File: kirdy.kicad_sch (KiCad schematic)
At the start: 0 parts

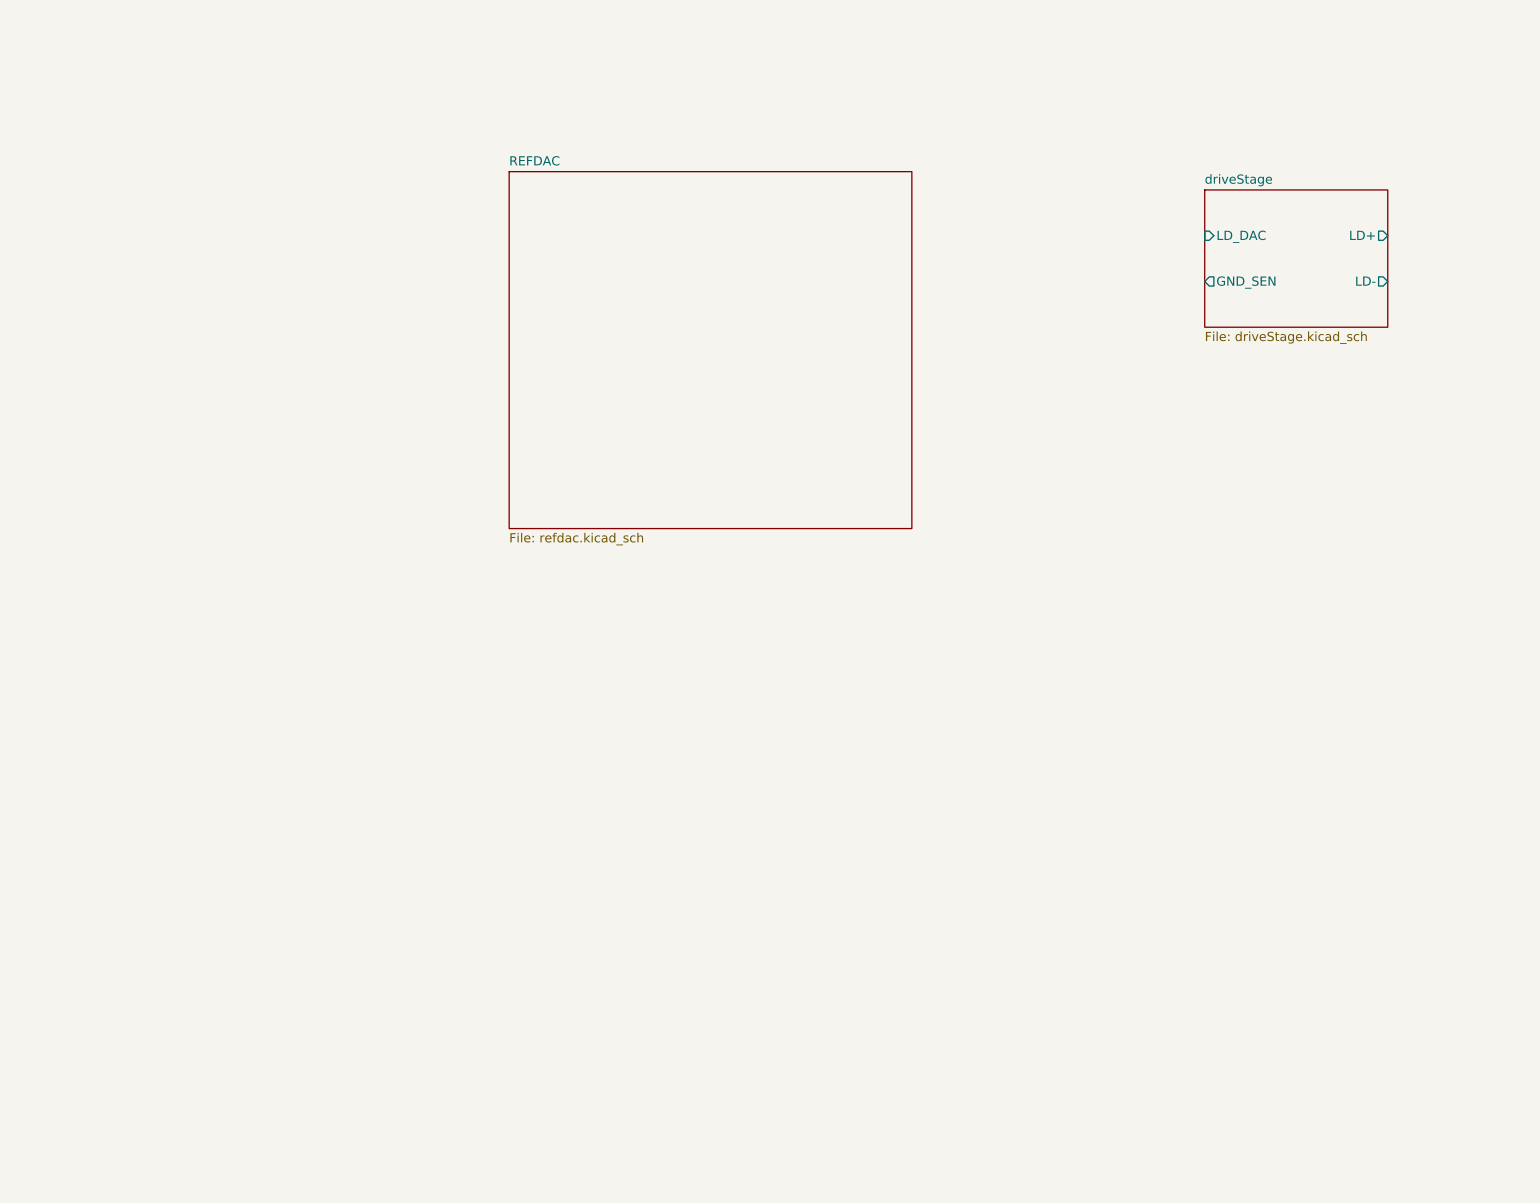
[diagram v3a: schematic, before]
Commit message: finish drive stage, add sheets
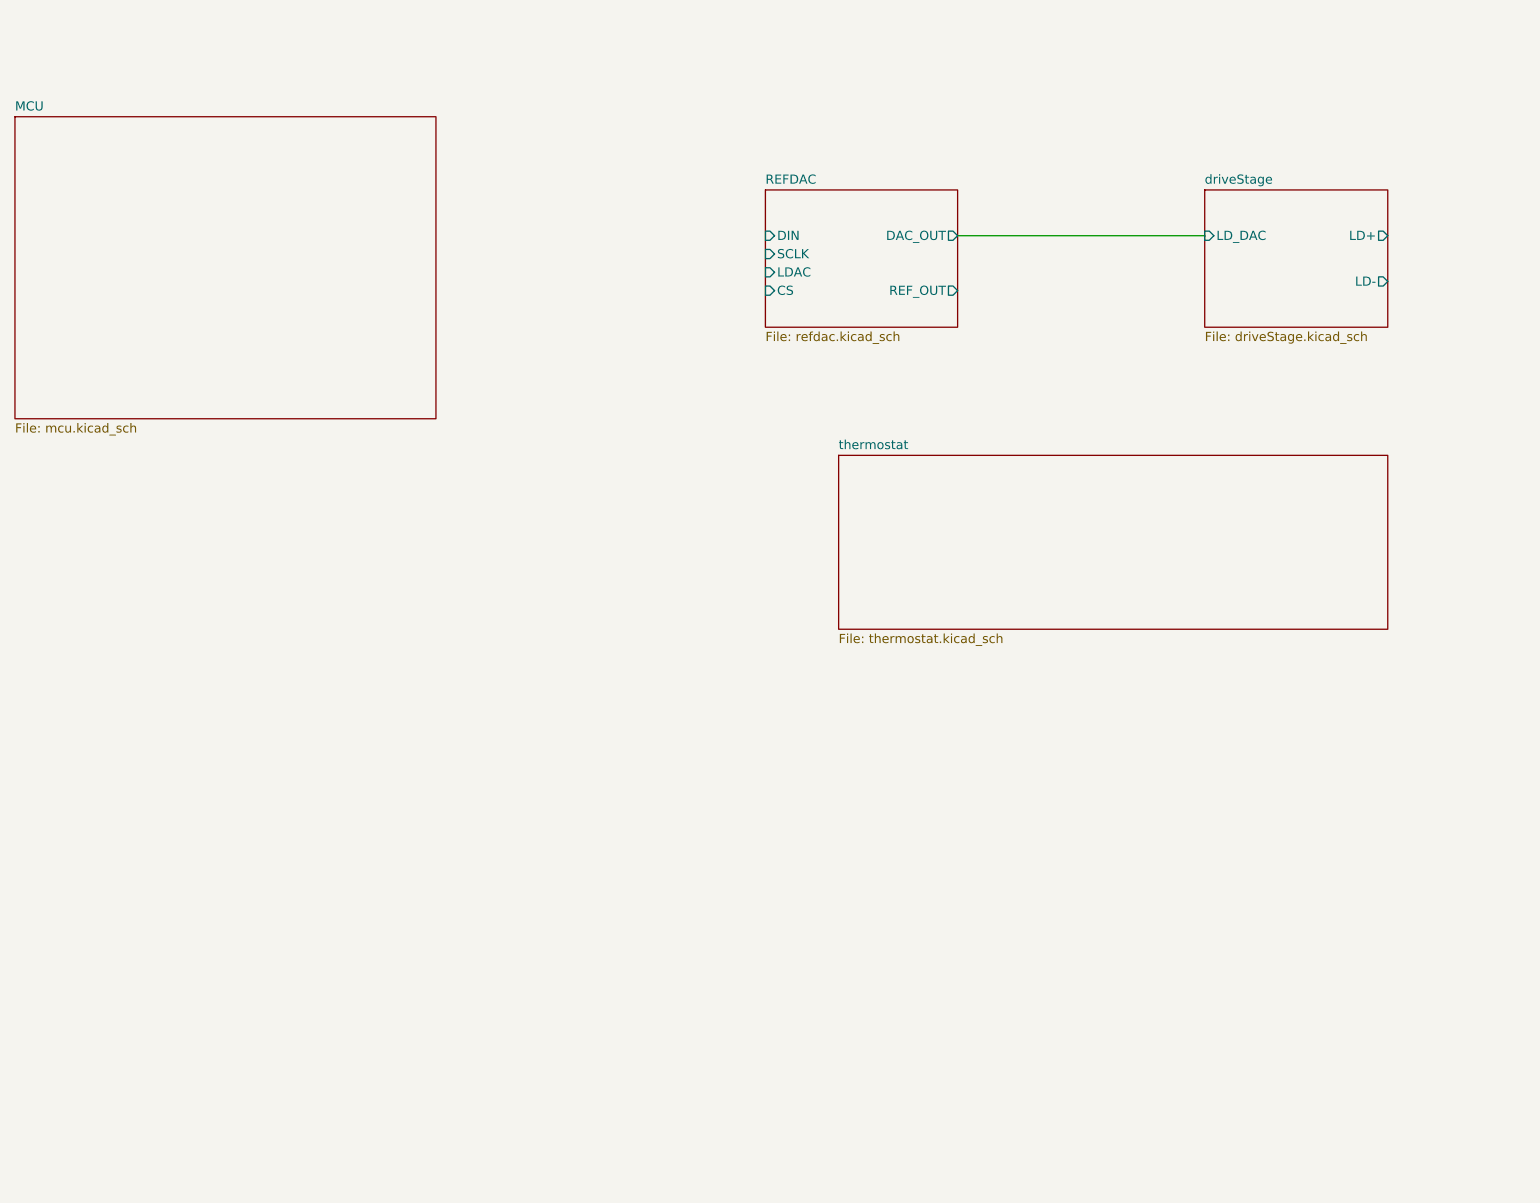
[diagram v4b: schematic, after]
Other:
- added sheet MCU (mcu.kicad_sch)
- added sheet thermostat (thermostat.kicad_sch)
- sheet REFDAC ports: added CS, DAC_OUT, DIN, LDAC, REF_OUT, SCLK; removed none
- sheet driveStage ports: added none; removed GND_SEN
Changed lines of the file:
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@@
 (kicad_sch (version 20211123) (generator eeschema)
   (paper "A3")
-  (sheet (at 173.99 91.44) (size 55.88 49.53) (fields_autoplaced)
-    (stroke (width 0.1524) (type solid) (color 0 0 0 0))
-    (fill (color 0 0 0 0.0000))
-    (property "Sheet name" "REFDAC" (id 0) (at 173.99 90.7284 0)
-      (effects (font (size 1.27 1.27)) (justify left bottom))
-    )
-    (property "Sheet file" "refdac.kicad_sch" (id 1) (at 173.99 141.5546 0)
-      (effects (font (size 1.27 1.27)) (justify left top))
+  (wire (pts (xy 236.22 100.33) (xy 270.51 100.33))
+    (stroke (width 0) (type default) (color 0 0 0 0))
+  )
+  (sheet (at 209.55 93.98) (size 26.67 19.05) (fields_autoplaced)
+    (stroke (width 0.1524) (type solid) (color 0 0 0 0))
+    (fill (color 0 0 0 0.0000))
+    (property "Sheet name" "REFDAC" (id 0) (at 209.55 93.2684 0)
+      (effects (font (size 1.27 1.27)) (justify left bottom))
+    )
+    (property "Sheet file" "refdac.kicad_sch" (id 1) (at 209.55 113.6146 0)
+      (effects (font (size 1.27 1.27)) (justify left top))
+    )
+    (pin "REF_OUT" output (at 236.22 107.95 0)
+      (effects (font (size 1.27 1.27)) (justify right))
+    )
+    (pin "DIN" input (at 209.55 100.33 180)
+      (effects (font (size 1.27 1.27)) (justify left))
+    )
+    (pin "SCLK" input (at 209.55 102.87 180)
+      (effects (font (size 1.27 1.27)) (justify left))
+    )
+    (pin "LDAC" input (at 209.55 105.41 180)
+      (effects (font (size 1.27 1.27)) (justify left))
+    )
+    (pin "CS" input (at 209.55 107.95 180)
+      (effects (font (size 1.27 1.27)) (justify left))
+    )
+    (pin "DAC_OUT" output (at 236.22 100.33 0)
+      (effects (font (size 1.27 1.27)) (justify right))
     )
   )
@@
       (effects (font (size 1.27 1.27)) (justify left top))
     )
-    (pin "GND_SEN" output (at 270.51 106.68 180)
-      (effects (font (size 1.27 1.27)) (justify left))
-    )
     (pin "LD-" output (at 295.91 106.68 0)
       (effects (font (size 1.27 1.27)) (justify right))
@@
     (pin "LD_DAC" input (at 270.51 100.33 180)
       (effects (font (size 1.27 1.27)) (justify left))
+    )
+  )
+  (sheet (at 219.71 130.81) (size 76.2 24.13) (fields_autoplaced)
+    (stroke (width 0.1524) (type solid) (color 0 0 0 0))
+    (fill (color 0 0 0 0.0000))
+    (property "Sheet name" "thermostat" (id 0) (at 219.71 130.0984 0)
+      (effects (font (size 1.27 1.27)) (justify left bottom))
+    )
+    (property "Sheet file" "thermostat.kicad_sch" (id 1) (at 219.71 155.5246 0)
+      (effects (font (size 1.27 1.27)) (justify left top))
+    )
+  )
+  (sheet (at 105.41 83.82) (size 58.42 41.91) (fields_autoplaced)
+    (stroke (width 0.1524) (type solid) (color 0 0 0 0))
+    (fill (color 0 0 0 0.0000))
+    (property "Sheet name" "MCU" (id 0) (at 105.41 83.1084 0)
+      (effects (font (size 1.27 1.27)) (justify left bottom))
+    )
+    (property "Sheet file" "mcu.kicad_sch" (id 1) (at 105.41 126.3146 0)
+      (effects (font (size 1.27 1.27)) (justify left top))
     )
   )
@@
     (path "/7fc2620b-bac4-49c0-a276-7d2a46898037" (page "2"))
     (path "/5c501399-91aa-4646-9dc0-aa6b782690af" (page "3"))
+    (path "/e9afb2cc-7f7f-4cb9-888a-0bfd71b1d070" (page "4"))
+    (path "/bda728c0-b189-4e05-8d4f-58a38acf883b" (page "5"))
   )
   (symbol_instances
@@
       (reference "#PWR?") (unit 1) (value "-6V") (footprint "")
     )
+    (path "/5c501399-91aa-4646-9dc0-aa6b782690af/3df7ecdc-b572-4de6-a82a-d6b5435d8510"
+      (reference "#PWR?") (unit 1) (value "+5VA") (footprint "")
+    )
     (path "/7fc2620b-bac4-49c0-a276-7d2a46898037/42e81420-64c1-4191-91f2-d9ce2b7f0c58"
       (reference "#PWR?") (unit 1) (value "GND") (footprint "")
     )
+    (path "/5c501399-91aa-4646-9dc0-aa6b782690af/4dba2aba-6f28-4797-ac3c-34562f8d224e"
+      (reference "#PWR?") (unit 1) (value "GND") (footprint "")
+    )
+    (path "/5c501399-91aa-4646-9dc0-aa6b782690af/5503d618-707a-4cba-ab38-dd469f3b3efe"
+      (reference "#PWR?") (unit 1) (value "+5VA") (footprint "")
+    )
     (path "/7fc2620b-bac4-49c0-a276-7d2a46898037/5f796a2f-98e9-46e3-a254-aaf7ea8e8609"
       (reference "#PWR?") (unit 1) (value "+9VA") (footprint "")
@@
     )
     (path "/7fc2620b-bac4-49c0-a276-7d2a46898037/7f2ae8de-9741-4de8-8b3e-0cbf1d496d0b"
+      (reference "#PWR?") (unit 1) (value "GND") (footprint "")
+    )
+    (path "/5c501399-91aa-4646-9dc0-aa6b782690af/81373c25-3cb4-4fd0-b5e3-926aada5cb12"
+      (reference "#PWR?") (unit 1) (value "GND") (footprint "")
+    )
+    (path "/5c501399-91aa-4646-9dc0-aa6b782690af/891cfc16-c51a-48dd-8b02-8066bd1e2772"
       (reference "#PWR?") (unit 1) (value "GND") (footprint "")
     )
@@
       (reference "#PWR?") (unit 1) (value "GND") (footprint "")
     )
+    (path "/5c501399-91aa-4646-9dc0-aa6b782690af/d4448496-e0b2-49ff-9c5d-1b88aa3e1c82"
+      (reference "#PWR?") (unit 1) (value "GND") (footprint "")
+    )
+    (path "/5c501399-91aa-4646-9dc0-aa6b782690af/d5c268d4-7f4e-42b6-9070-6d2fbae6ea5b"
+      (reference "#PWR?") (unit 1) (value "GND") (footprint "")
+    )
     (path "/7fc2620b-bac4-49c0-a276-7d2a46898037/d79107b5-7dc2-415e-945e-ed09fd9cfe77"
       (reference "#PWR?") (unit 1) (value "-6V") (footprint "")
@@
       (reference "C?") (unit 1) (value "10n") (footprint "")
     )
+    (path "/5c501399-91aa-4646-9dc0-aa6b782690af/5d906de7-2bb4-4b20-96f3-f31e23e911d5"
+      (reference "C?") (unit 1) (value "100n") (footprint "")
+    )
     (path "/7fc2620b-bac4-49c0-a276-7d2a46898037/6515a0cc-09fd-42e3-8559-ed97c2e10919"
       (reference "C?") (unit 1) (value "100n") (footprint "")
     )
+    (path "/5c501399-91aa-4646-9dc0-aa6b782690af/7c87fd56-71ea-4cb6-b34c-128457749b5d"
+      (reference "C?") (unit 1) (value "10u") (footprint "")
+    )
     (path "/7fc2620b-bac4-49c0-a276-7d2a46898037/7d6a0bc2-603a-43a2-992b-4f35cbb0a1f8"
+      (reference "C?") (unit 1) (value "100n") (footprint "")
+    )
+    (path "/5c501399-91aa-4646-9dc0-aa6b782690af/8d327d8f-666a-4058-810c-d69eb17ab4c1"
       (reference "C?") (unit 1) (value "100n") (footprint "")
     )
@@
       (reference "C?") (unit 1) (value "10u") (footprint "")
     )
+    (path "/5c501399-91aa-4646-9dc0-aa6b782690af/b18eacc1-67e7-4eec-9489-8009080dc8c2"
+      (reference "C?") (unit 1) (value "1u") (footprint "")
+    )
     (path "/7fc2620b-bac4-49c0-a276-7d2a46898037/cf733f3d-f3a4-44f4-a550-52da39242bf1"

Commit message: remove ref dac sheet, finish thermostat
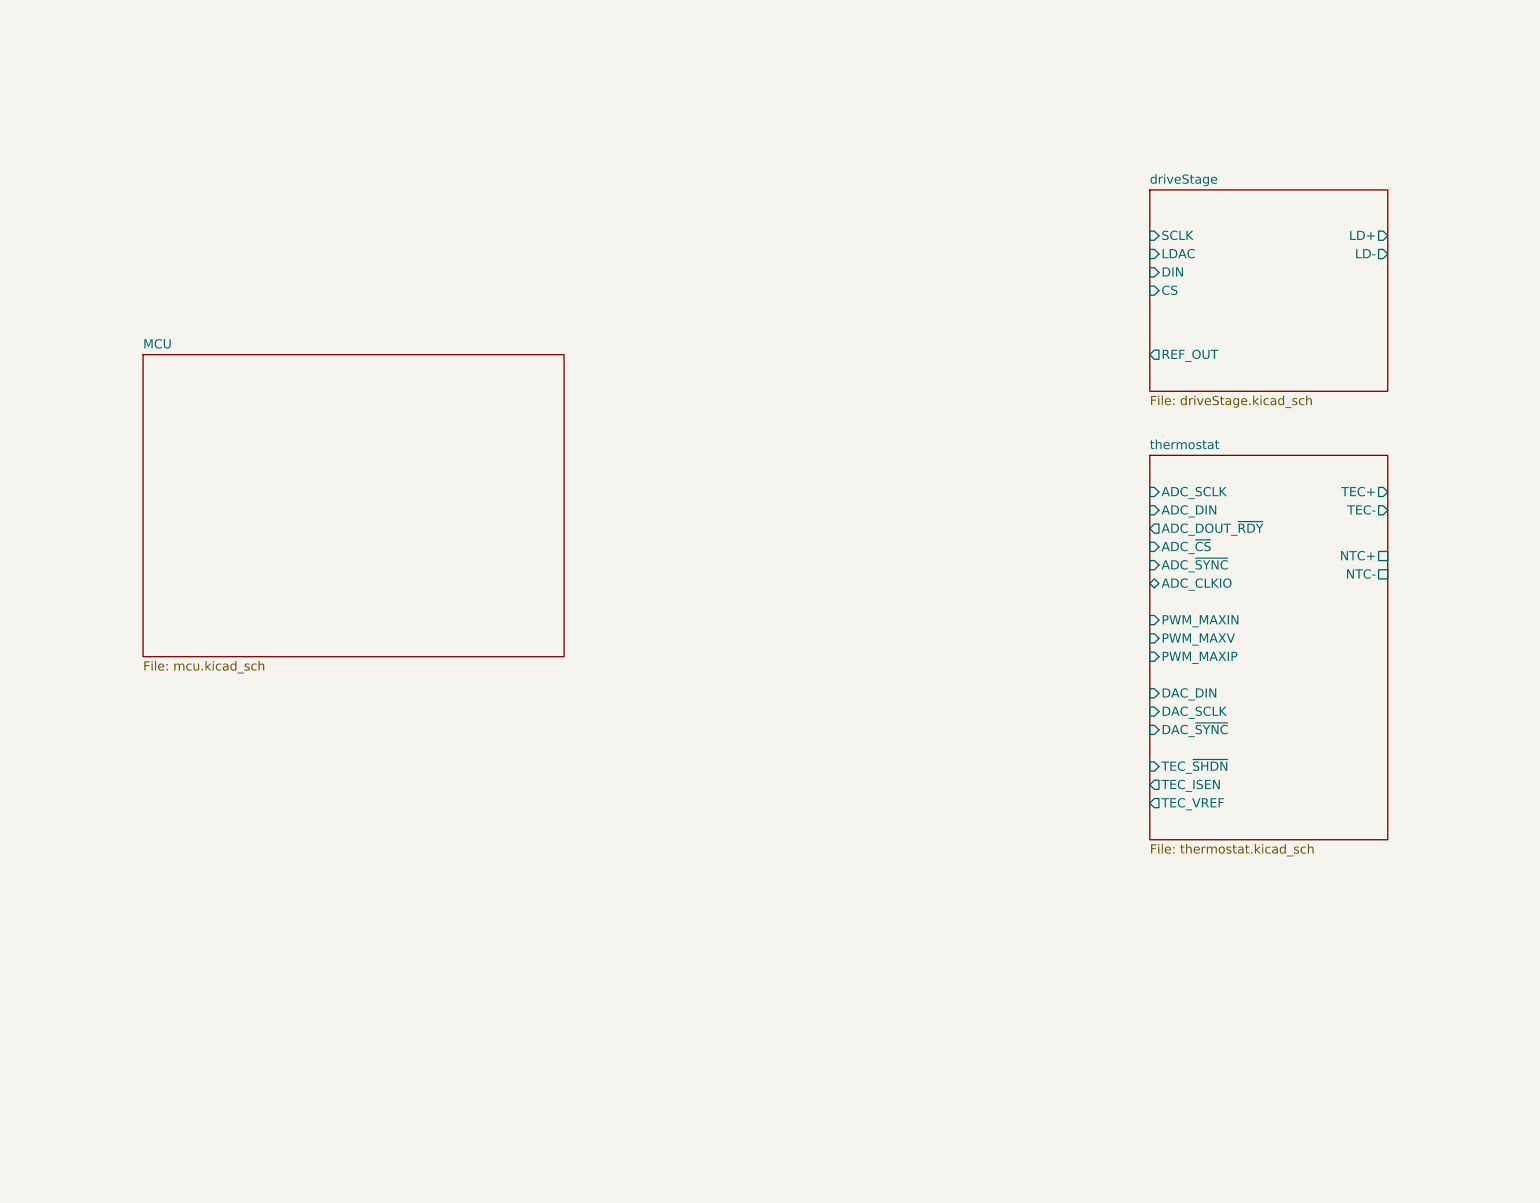
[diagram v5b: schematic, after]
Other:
- removed sheet REFDAC
- sheet driveStage ports: added CS, DIN, LDAC, REF_OUT, SCLK; removed LD_DAC
- sheet thermostat ports: added ADC_CLKIO, ADC_DIN, ADC_DOUT_~{RDY}, ADC_SCLK, ADC_~{CS}, ADC_~{SYNC}, DAC_DIN, DAC_SCLK, DAC_~{SYNC}, NTC+, NTC-, PWM_MAXIN, PWM_MAXIP, PWM_MAXV, TEC+, TEC-, TEC_ISEN, TEC_VREF, TEC_~{SHDN}; removed none
